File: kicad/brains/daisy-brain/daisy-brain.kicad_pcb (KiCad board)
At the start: 2 copper layers, 36 x 54 mm, 6 parts, among them J15 Conn_01x06, J16 Conn_01x06, J17 Conn_01x06, J18 Conn_01x06, J4 Conn_02x20_Odd_Even, J5 Conn_02x20_Odd_Even

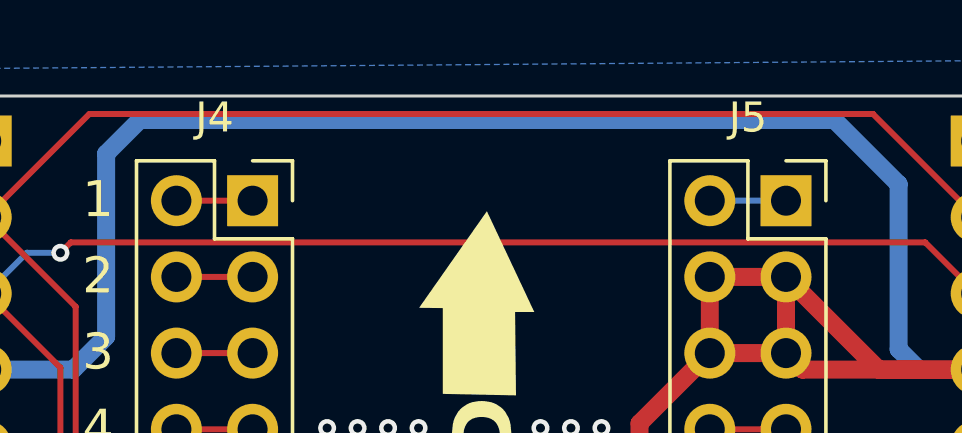
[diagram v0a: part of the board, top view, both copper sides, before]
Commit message: Update card template and MIDI Buddy
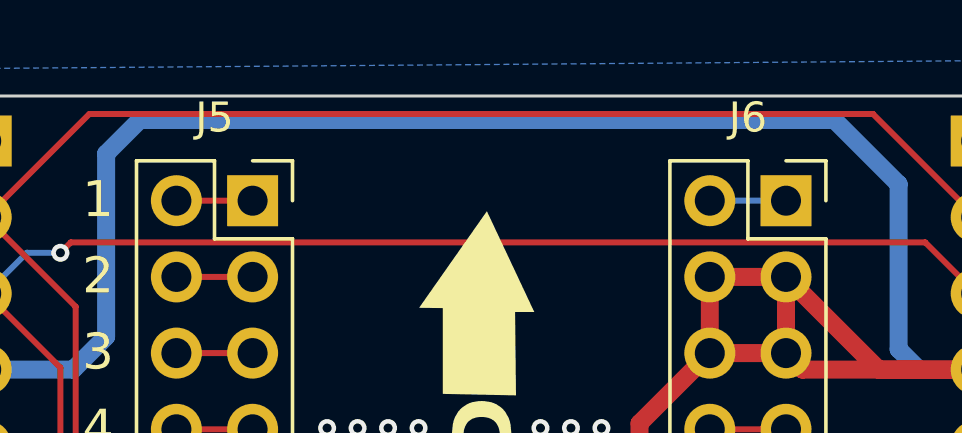
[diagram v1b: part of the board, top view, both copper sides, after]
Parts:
- renumbered J15 to J1, J16 to J2, J17 to J3, J18 to J4, J4 to J5, J5 to J6
